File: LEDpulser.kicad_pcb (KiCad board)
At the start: 2 copper layers, 38.2 x 98.2 mm, 61 parts, among them J1 RJ45_Shielded, J2 EPS.00.250.NTN, J3 EPS.00.250.NTN, J4 Conn_01x04_Female, J5 LED, Q1 AO3401A, Q2 AO3400A, Q3 AO3400A, SW1 ATE1D-5M3-10-Z, U1 74HC123, U10 LT3082, U2 74HC123, U3 74HC123, U4 74HC10, U5 LT1121-5, U6 PM8834, U7 NE555, U8 PM8834, U9 PM8834

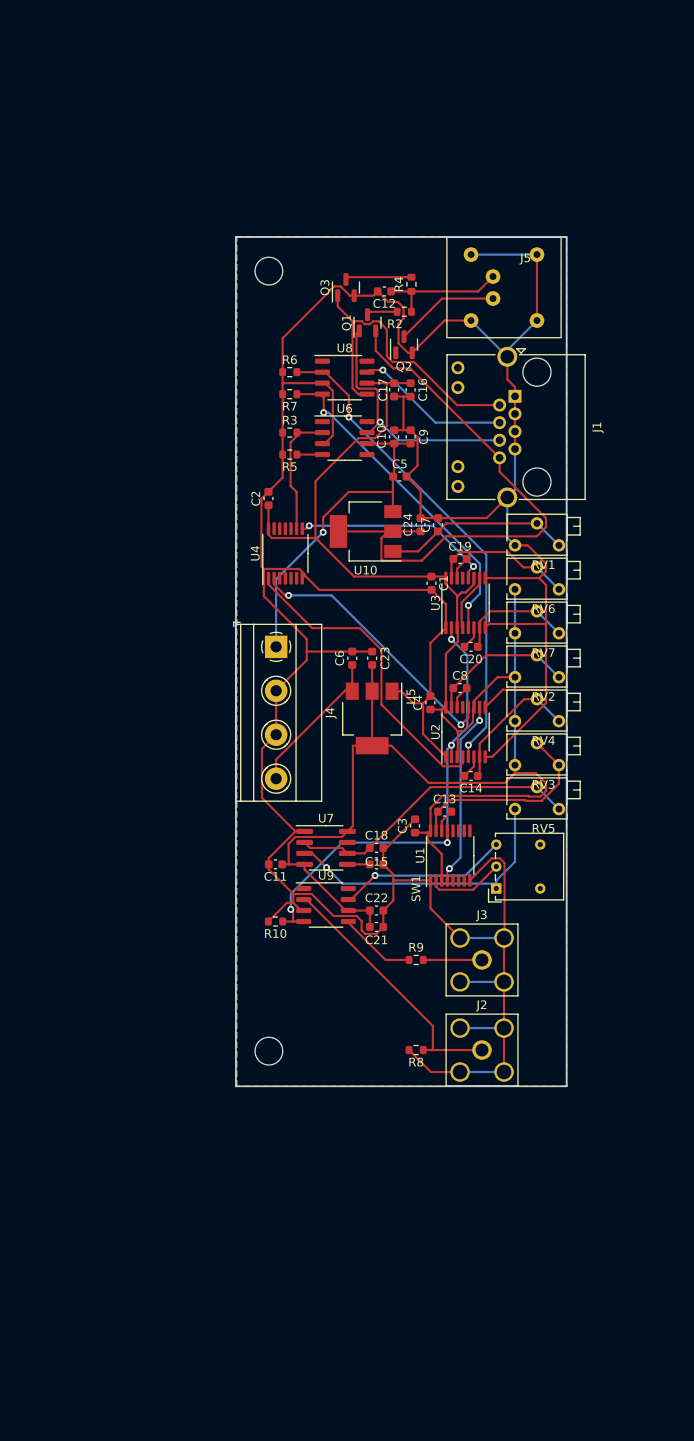
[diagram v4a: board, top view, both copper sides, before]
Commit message: Fixed open connection, grounded unused inputs, adjusted connector facing.
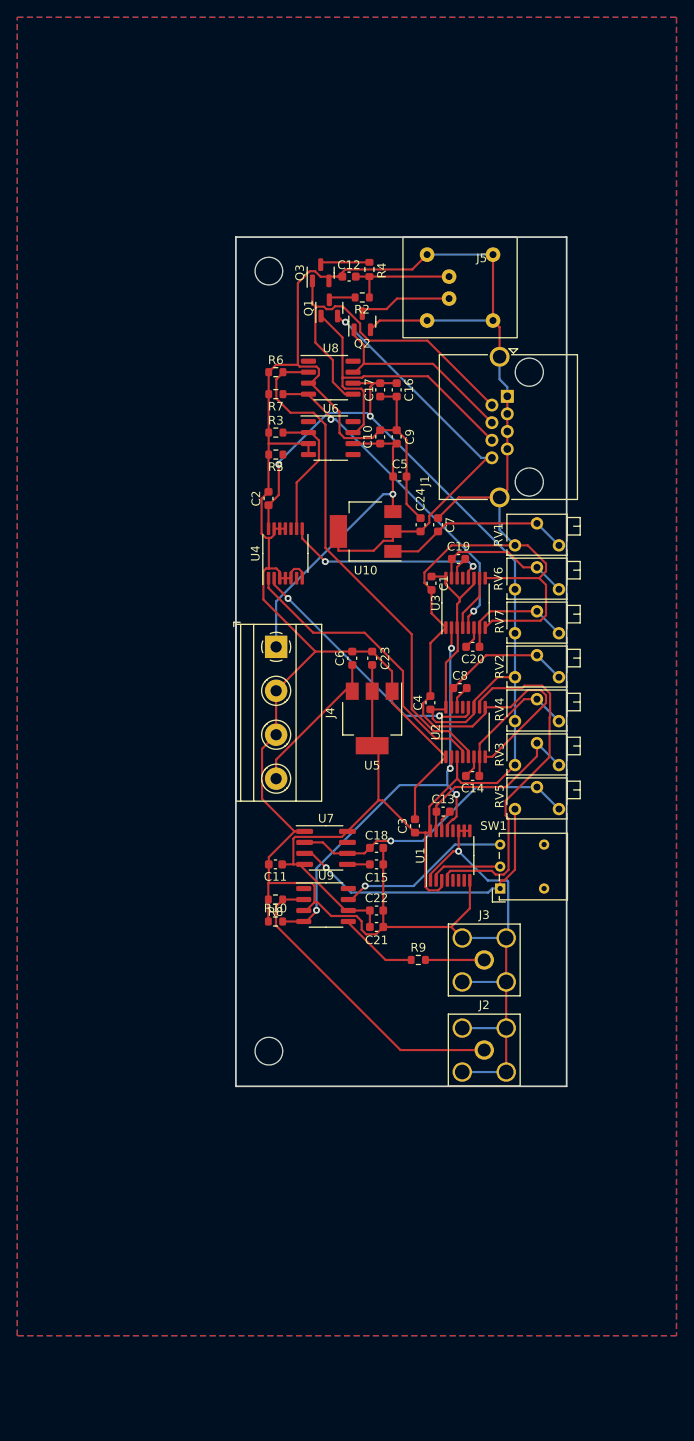
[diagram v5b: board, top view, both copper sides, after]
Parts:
- J1: value RJ45_Shielded -> RJHSE5380; footprint Connector_RJ:RJ45_Amphenol_RJHSE538X -> Connector_RJ:RJ45_Amphenol_RJHSE5380
- R8: value 50 -> 100k
- moved R8 23.8 mm to (106.0, 102.0)
- moved Q2 5.51 mm to (116.1, 35.2)
- moved R4 5.15 mm to (116.9, 29.1)
- moved R2 5.13 mm to (116.1, 32.4)
- moved J5 5.08 mm to (127.4, 31.2)
- moved Q1 4.73 mm to (112.3, 33.6)
- moved C12 4.43 mm to (114.6, 30.0)
- moved Q3 3.39 mm to (111.3, 29.5)
- moved U6 1.61 mm to (112.4, 48.6)
- moved U8 1.61 mm to (112.4, 41.7)
- moved C10 1.61 mm to (118.1, 48.5)
- moved C16 1.61 mm to (120.1, 43.1)
- moved C17 1.61 mm to (118.1, 43.1)
- moved C9 1.61 mm to (120.1, 48.5)
- moved R3 1.61 mm to (106.1, 48.0)
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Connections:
- Q2 pad 1: unconnected-(Q2-Pad1) -> /LED_ON
- U1 pad 10: (no net) -> GND
- U1 pad 11: (no net) -> GND
- U1 pad 12: (no net) -> unconnected-(U1-Pad12)
- U1 pad 5: (no net) -> unconnected-(U1-Pad5)
- U1 pad 6: (no net) -> unconnected-(U1-Pad6)
- U1 pad 7: (no net) -> unconnected-(U1-Pad7)
- U1 pad 9: (no net) -> GND
- U4 pad 10: (no net) -> unconnected-(U4-Pad10)
- U4 pad 11: (no net) -> GND
- U4 pad 12: (no net) -> GND
- U4 pad 13: (no net) -> GND
- U4 pad 3: (no net) -> GND
- U4 pad 4: (no net) -> GND
- U4 pad 5: (no net) -> GND
- U4 pad 6: (no net) -> unconnected-(U4-Pad6)
- U6 pad 4: Net-(R5-Pad1) -> GND
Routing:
- net GND: track 410.9 -> 438.8 mm, vias 0 -> 1
- net Net-(U1-Pad4): track 21.6 -> 41.0 mm, vias 2 -> 0
- net /CAP_VOLTAGE: track 65.7 -> 50.1 mm, vias 0 -> 1
- net +5V: track 207.9 -> 195.5 mm, vias 0 -> 2
- net /CAP_CHARGE: track 29.7 -> 37.7 mm, vias 1 -> 0
- net /LED_ON: track 17.9 -> 23.7 mm, vias 1 -> 0
- net /EXT: track 30.6 -> 35.8 mm
- net /LED_SHORT: track 36.5 -> 41.5 mm
- net Net-(R6-Pad1): track 56.3 -> 59.5 mm, vias 2 -> 0
- net Net-(R5-Pad1): track 2.95 -> 0.00 mm
- net +12V: track 39.5 -> 37.0 mm
- net Net-(U2-Pad4): track 36.5 -> 34.4 mm
- net Net-(Q3-Pad3): track 7.68 -> 5.90 mm
- net Net-(C12-Pad1): track 14.8 -> 13.2 mm
- net Net-(C13-Pad1): track 23.4 -> 22.0 mm
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
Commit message: reverting back to last commit
hopefuly reverting back to last commit pls
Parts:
- J1: value RJHSE5380 -> RJ45_Shielded; footprint Connector_RJ:RJ45_Amphenol_RJHSE5380 -> Connector_RJ:RJ45_Amphenol_RJHSE538X
- R8: value 100k -> 50
- moved R8 23.8 mm to (122.3, 119.4)
- moved Q2 5.51 mm to (120.9, 37.8)
- moved R4 5.15 mm to (121.8, 30.9)
- moved R2 5.13 mm to (120.9, 34.0)
- moved J5 5.08 mm to (132.5, 31.2)
- moved Q1 4.73 mm to (116.7, 35.3)
- moved C12 4.43 mm to (118.6, 31.7)
- moved Q3 3.39 mm to (114.2, 31.2)
- moved U6 1.61 mm to (114.0, 48.6)
- moved U8 1.61 mm to (114.0, 41.7)
- moved C10 1.61 mm to (119.8, 48.5)
- moved C16 1.61 mm to (121.7, 43.1)
- moved C17 1.61 mm to (119.8, 43.1)
- moved C9 1.61 mm to (121.7, 48.5)
- moved R3 1.61 mm to (107.7, 48.0)
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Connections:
- Q2 pad 1: /LED_ON -> unconnected-(Q2-Pad1)
- U1 pad 10: GND -> (no net)
- U1 pad 11: GND -> (no net)
- U1 pad 12: unconnected-(U1-Pad12) -> (no net)
- U1 pad 5: unconnected-(U1-Pad5) -> (no net)
- U1 pad 6: unconnected-(U1-Pad6) -> (no net)
- U1 pad 7: unconnected-(U1-Pad7) -> (no net)
- U1 pad 9: GND -> (no net)
- U4 pad 10: unconnected-(U4-Pad10) -> (no net)
- U4 pad 11: GND -> (no net)
- U4 pad 12: GND -> (no net)
- U4 pad 13: GND -> (no net)
- U4 pad 3: GND -> (no net)
- U4 pad 4: GND -> (no net)
- U4 pad 5: GND -> (no net)
- U4 pad 6: unconnected-(U4-Pad6) -> (no net)
- U6 pad 4: GND -> Net-(R5-Pad1)
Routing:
- net GND: track 438.8 -> 410.9 mm, vias 1 -> 0
- net Net-(U1-Pad4): track 41.0 -> 21.6 mm, vias 0 -> 2
- net /CAP_VOLTAGE: track 50.1 -> 65.7 mm, vias 1 -> 0
- net +5V: track 195.5 -> 207.9 mm, vias 2 -> 0
- net /CAP_CHARGE: track 37.7 -> 29.7 mm, vias 0 -> 1
- net /LED_ON: track 23.7 -> 17.9 mm, vias 0 -> 1
- net /EXT: track 35.8 -> 30.6 mm
- net /LED_SHORT: track 41.5 -> 36.5 mm
- net Net-(R6-Pad1): track 59.5 -> 56.3 mm, vias 0 -> 2
- net Net-(R5-Pad1): track 0.00 -> 2.95 mm
- net +12V: track 37.0 -> 39.5 mm
- net Net-(U2-Pad4): track 34.4 -> 36.5 mm
- net Net-(Q3-Pad3): track 5.90 -> 7.68 mm
- net Net-(C12-Pad1): track 13.2 -> 14.8 mm
- net Net-(C13-Pad1): track 22.0 -> 23.4 mm
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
